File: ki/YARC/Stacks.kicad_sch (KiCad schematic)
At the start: 0 parts

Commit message: Ongoing schematic changes
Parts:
- added U201, U204, U207, U209: 74LS670, symbol 74xx:74LS670
- added U202, U205, U208, U210: 74LS283, symbol 74xx:74LS283
- added U203, U206: 74LS574, symbol 74xx:74LS574
- added U211, U212, U213, U214: 74LS245, symbol 74xx:74LS245
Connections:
- new net: U208.9 (C4), U210.7 (C0)
- new net: U202.9 (C4), U205.7 (C0)
- new net ACN0: U201.14 (Wa), U201.5 (Ra), U204.14 (Wa), U204.5 (Ra), U207.14 (Wa), U207.5 (Ra), U209.14 (Wa), U209.5 (Ra)
- new net ACN1: U201.13 (Wb), U201.4 (Rb), U204.13 (Wb), U204.4 (Rb), U207.13 (Wb), U207.4 (Rb), U209.13 (Wb), U209.4 (Rb)
- new net ALUOUT0: U211.2 (A0)
- new net ALUOUT1: U211.3 (A1)
- new net ALUOUT10: U212.4 (A2)
- new net ALUOUT11: U212.5 (A3)
- new net ALUOUT12: U212.6 (A4)
- new net ALUOUT13: U212.7 (A5)
- new net ALUOUT14: U212.8 (A6)
- new net ALUOUT15: U212.9 (A7)
- new net ALUOUT2: U211.4 (A2)
- new net ALUOUT3: U211.5 (A3)
- new net ALUOUT4: U211.6 (A4)
- new net ALUOUT5: U211.7 (A5)
- new net ALUOUT6: U211.8 (A6)
- new net ALUOUT7: U211.9 (A7)
- new net ALUOUT8: U212.2 (A0)
- new net ALUOUT9: U212.3 (A1)
- new net C8: U205.9 (C4), U208.7 (C0)
- new net GND: U201.8 (GND), U202.7 (C0), U202.8 (GND), U203.1 (OE), U203.10 (GND), U204.8 (GND), U205.8 (GND), U206.1 (OE), U206.10 (GND), U207.8 (GND), U208.8 (GND), U209.8 (GND), U210.8 (GND), U211.10 (GND), U212.10 (GND), U213.10 (GND), U214.10 (GND)
- new net HOLD0: U201.15 (D1), U203.19 (Q0)
- new net HOLD1: U201.1 (D2), U203.18 (Q1)
- new net HOLD10: U206.17 (Q2), U207.2 (D3)
- new net HOLD11: U206.16 (Q3), U207.3 (D4)
- new net HOLD12: U206.15 (Q4), U209.15 (D1)
- new net HOLD13: U206.14 (Q5), U209.1 (D2)
- new net HOLD14: U206.13 (Q6), U209.2 (D3)
- new net HOLD15: U206.12 (Q7), U209.3 (D4)
- new net HOLD2: U201.2 (D3), U203.17 (Q2)
- new net HOLD3: U201.3 (D4), U203.16 (Q3)
- new net HOLD4: U203.15 (Q4), U204.15 (D1)
- new net HOLD5: U203.14 (Q5), U204.1 (D2)
- new net HOLD6: U203.13 (Q6), U204.2 (D3)
- new net HOLD7: U203.12 (Q7), U204.3 (D4)
- new net HOLD8: U206.19 (Q0), U207.15 (D1)
- new net HOLD9: U206.18 (Q1), U207.1 (D2)
- new net SRC2:0: U202.6 (B1)
- new net SRC2:1: U202.2 (B2)
- new net SRC2:2: U202.11 (B4), U202.15 (B3), U205.11 (B4), U205.15 (B3), U205.2 (B2), U205.6 (B1), U208.11 (B4), U208.15 (B3), U208.2 (B2), U208.6 (B1), U210.11 (B4), U210.15 (B3), U210.2 (B2), U210.6 (B1)
- new net SUM0: U202.4 (S1), U203.2 (D0)
- new net SUM1: U202.1 (S2), U203.3 (D1)
- new net SUM10: U206.4 (D2), U208.13 (S3)
- new net SUM11: U206.5 (D3), U208.10 (S4)
- new net SUM12: U206.6 (D4), U210.4 (S1)
- new net SUM13: U206.7 (D5), U210.1 (S2)
- new net SUM14: U206.8 (D6), U210.13 (S3)
- new net SUM15: U206.9 (D7), U210.10 (S4)
- new net SUM2: U202.13 (S3), U203.4 (D2)
- new net SUM3: U202.10 (S4), U203.5 (D3)
- new net SUM4: U203.6 (D4), U205.4 (S1)
- new net SUM5: U203.7 (D5), U205.1 (S2)
- new net SUM6: U203.8 (D6), U205.13 (S3)
- new net SUM7: U203.9 (D7), U205.10 (S4)
- new net SUM8: U206.2 (D0), U208.4 (S1)
- new net SUM9: U206.3 (D1), U208.1 (S2)
- new net SYSADDR0: U201.10 (Q1), U202.5 (A1), U211.18 (B0), U214.11 (B7)
- new net SYSADDR1: U201.9 (Q2), U202.3 (A2), U211.17 (B1), U214.12 (B6)
- new net SYSADDR10: U207.7 (Q3), U208.14 (A3), U212.16 (B2), U213.13 (B5)
- new net SYSADDR11: U207.6 (Q4), U208.12 (A4), U212.15 (B3), U213.14 (B4)
- new net SYSADDR12: U209.10 (Q1), U210.5 (A1), U212.14 (B4), U213.15 (B3)
- new net SYSADDR13: U209.9 (Q2), U210.3 (A2), U212.13 (B5), U213.16 (B2)
- new net SYSADDR14: U209.7 (Q3), U210.14 (A3), U212.12 (B6), U213.17 (B1)
- new net SYSADDR15: U209.6 (Q4), U210.12 (A4), U212.11 (B7), U213.18 (B0)
- new net SYSADDR2: U201.7 (Q3), U202.14 (A3), U211.16 (B2), U214.13 (B5)
- new net SYSADDR3: U201.6 (Q4), U202.12 (A4), U211.15 (B3), U214.14 (B4)
- new net SYSADDR4: U204.10 (Q1), U205.5 (A1), U211.14 (B4), U214.15 (B3)
- new net SYSADDR5: U204.9 (Q2), U205.3 (A2), U211.13 (B5), U214.16 (B2)
- new net SYSADDR6: U204.7 (Q3), U205.14 (A3), U211.12 (B6), U214.17 (B1)
- new net SYSADDR7: U204.6 (Q4), U205.12 (A4), U211.11 (B7), U214.18 (B0)
- new net SYSADDR8: U207.10 (Q1), U208.5 (A1), U212.18 (B0), U213.11 (B7)
- new net SYSADDR9: U207.9 (Q2), U208.3 (A2), U212.17 (B1), U213.12 (B6)
- new net SYSCLK: U203.11 (Cp), U206.11 (Cp)
- new net SYSDATA0: U214.9 (A7)
- new net SYSDATA1: U214.8 (A6)
- new net SYSDATA10: U213.7 (A5)
- new net SYSDATA11: U213.6 (A4)
- new net SYSDATA12: U213.5 (A3)
- new net SYSDATA13: U213.4 (A2)
- new net SYSDATA14: U213.3 (A1)
- new net SYSDATA15: U213.2 (A0)
- new net SYSDATA2: U214.7 (A5)
- new net SYSDATA3: U214.6 (A4)
- new net SYSDATA4: U214.5 (A3)
- new net SYSDATA5: U214.4 (A2)
- new net SYSDATA6: U214.3 (A1)
- new net SYSDATA7: U214.2 (A0)
- new net SYSDATA8: U213.9 (A7)
- new net SYSDATA9: U213.8 (A6)
- new net VCC: U201.16 (VCC), U202.16 (VCC), U203.20 (VCC), U204.16 (VCC), U205.16 (VCC), U206.20 (VCC), U207.16 (VCC), U208.16 (VCC), U209.16 (VCC), U210.16 (VCC), U211.1 (A->B), U211.20 (VCC), U212.1 (A->B), U212.20 (VCC), U213.1 (A->B), U213.20 (VCC), U214.1 (A->B), U214.20 (VCC)
- new net ~{ALUtoA}: U211.19 (CE), U212.19 (CE)
- new net ~{DtoA}: U213.19 (CE), U214.19 (CE)
- new net ~{IXRD}: U201.11 (~{Er}), U204.11 (~{Er}), U207.11 (~{Er}), U209.11 (~{Er})
- new net ~{IXWR}: U201.12 (~{Ew}), U204.12 (~{Ew}), U207.12 (~{Ew}), U209.12 (~{Ew})
- no-connect marks 0 -> 1
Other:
- note added: "The U200-numbered ICs on this page match the low digits of the U numbers on the V503 Addressing Unit circuit board. U207 on this page is U7 on the circuit board, etc. Other names match the V503 schematic where possible but all match the naming here in the YARC schematic."
- title: YARC Stacks -> YARC Addressing Unit (AU)

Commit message: Schematic for addressing unit is complete and all ERC violations addressed
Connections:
- net ~{ALUtoA} renamed ~{ADDR_ALU}
- net ~{DtoA} renamed ~{SYSDATA_SRC_IS_A}

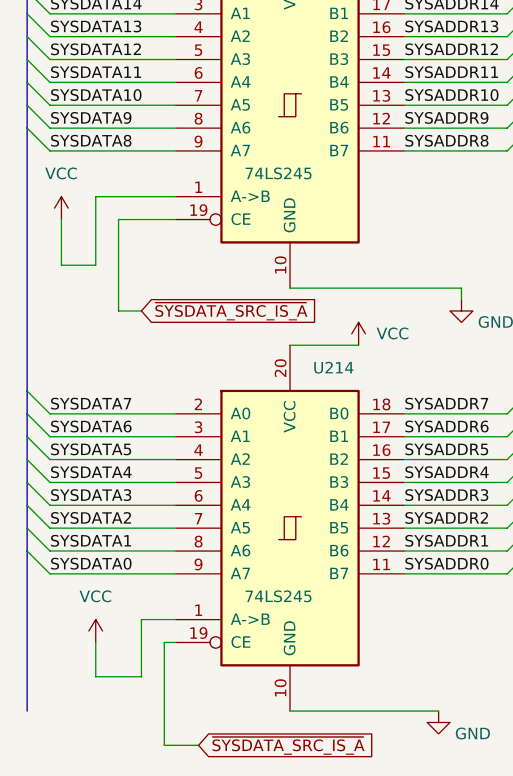
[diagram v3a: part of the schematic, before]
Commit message: Revise SET# logic for LD_UCODE_CTR#. Fix minor errors with no functional consequences (schematic didn't match reality)
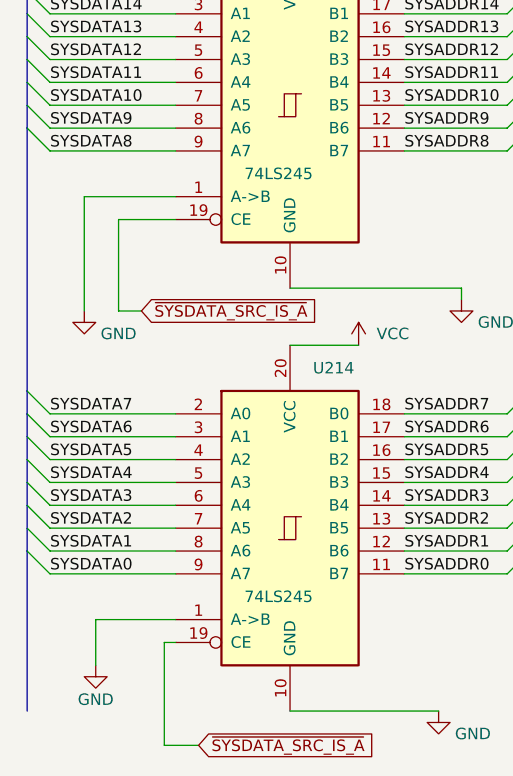
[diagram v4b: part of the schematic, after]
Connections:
- net GND: now also U213.1 (A->B), U214.1 (A->B)
- net VCC: no longer U213.1 (A->B), U214.1 (A->B)
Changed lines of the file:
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@@
     (stroke (width 0) (type default))
   )
-  (wire (pts (xy 29.21 187.96) (xy 25.4 187.96))
+  (wire (pts (xy 29.21 187.96) (xy 20.32 187.96))
     (stroke (width 0) (type default))
   )
@@
     (stroke (width 0) (type default))
   )
-  (wire (pts (xy 20.32 140.97) (xy 20.32 148.59))
-    (stroke (width 0) (type default))
-  )
   (bus (pts (xy 207.01 72.39) (xy 207.01 74.93))
     (stroke (width 0) (type default))
@@
     (stroke (width 0) (type default))
   )
-  (wire (pts (xy 20.32 148.59) (xy 16.51 148.59))
-    (stroke (width 0) (type default))
-  )
   (bus (pts (xy 12.7 172.72) (xy 12.7 175.26))
     (stroke (width 0) (type default))
@@
     (stroke (width 0) (type default))
   )
+  (wire (pts (xy 19.05 140.97) (xy 19.05 153.67))
+    (stroke (width 0) (type default))
+  )
   (wire (pts (xy 173.99 116.84) (xy 173.99 129.54))
     (stroke (width 0) (type default))
@@
     (stroke (width 0) (type default))
   )
-  (wire (pts (xy 16.51 143.51) (xy 16.51 148.59))
-    (stroke (width 0) (type default))
-  )
   (bus (pts (xy 147.32 25.4) (xy 147.32 27.94))
     (stroke (width 0) (type default))
@@
     (stroke (width 0) (type default))
   )
-  (wire (pts (xy 20.32 190.5) (xy 20.32 194.31))
-    (stroke (width 0) (type default))
-  )
   (wire (pts (xy 15.24 133.35) (xy 29.21 133.35))
     (stroke (width 0) (type default))
@@
     (stroke (width 0) (type default))
   )
-  (wire (pts (xy 25.4 187.96) (xy 25.4 194.31))
+  (wire (pts (xy 20.32 187.96) (xy 20.32 193.04))
     (stroke (width 0) (type default))
   )
@@
     (stroke (width 0) (type default))
   )
-  (wire (pts (xy 20.32 140.97) (xy 29.21 140.97))
+  (wire (pts (xy 19.05 140.97) (xy 29.21 140.97))
     (stroke (width 0) (type default))
   )
@@
   )
   (bus (pts (xy 266.7 25.4) (xy 266.7 27.94))
-    (stroke (width 0) (type default))
-  )
-  (wire (pts (xy 25.4 194.31) (xy 20.32 194.31))
     (stroke (width 0) (type default))
   )
@@
     )
   )
+  (symbol (lib_id "power:GND") (at 19.05 153.67 0) (unit 1)
+    (in_bom yes) (on_board yes) (dnp no)
+    (property "Reference" "#PWR0249" (at 19.05 160.02 0)
+      (effects (font (size 1.27 1.27)) hide)
+    )
+    (property "Value" "GND" (at 22.86 156.21 0)
+      (effects (font (size 1.27 1.27)))
+    )
+    (property "Footprint" "" (at 19.05 153.67 0)
+      (effects (font (size 1.27 1.27)) hide)
+    )
+    (property "Datasheet" "" (at 19.05 153.67 0)
+      (effects (font (size 1.27 1.27)) hide)
+    )
+    (pin "1")
+    (instances
+      (project "YARC"
+        (path "/22e0f8e1-b0d7-4d47-bb7c-8ef04cd95fca/ab31a2b6-5416-47ce-a658-779ff6faeebe"
+          (reference "#PWR0249") (unit 1)
+        )
+      )
+    )
+  )
   (symbol (lib_id "power:GND") (at 232.41 63.5 0) (unit 1)
     (in_bom yes) (on_board yes) (dnp no) (fields_autoplaced)
@@
     )
   )
+  (symbol (lib_id "power:GND") (at 20.32 193.04 0) (unit 1)
+    (in_bom yes) (on_board yes) (dnp no)
+    (property "Reference" "#PWR0160" (at 20.32 199.39 0)
+      (effects (font (size 1.27 1.27)) hide)
+    )
+    (property "Value" "GND" (at 20.32 196.85 0)
+      (effects (font (size 1.27 1.27)))
+    )
+    (property "Footprint" "" (at 20.32 193.04 0)
+      (effects (font (size 1.27 1.27)) hide)
+    )
+    (property "Datasheet" "" (at 20.32 193.04 0)
+      (effects (font (size 1.27 1.27)) hide)
+    )
+    (pin "1")
+    (instances
+      (project "YARC"
+        (path "/22e0f8e1-b0d7-4d47-bb7c-8ef04cd95fca/ab31a2b6-5416-47ce-a658-779ff6faeebe"
+          (reference "#PWR0160") (unit 1)
+        )
+      )
+    )
+  )
   (symbol (lib_id "power:GND") (at 153.67 143.51 0) (unit 1)
     (in_bom yes) (on_board yes) (dnp no) (fields_autoplaced)
@@
         (path "/22e0f8e1-b0d7-4d47-bb7c-8ef04cd95fca/ab31a2b6-5416-47ce-a658-779ff6faeebe"
           (reference "U210") (unit 1)
-        )
-      )
-    )
-  )
-  (symbol (lib_id "power:VCC") (at 20.32 190.5 0) (unit 1)
-    (in_bom yes) (on_board yes) (dnp no) (fields_autoplaced)
-    (property "Reference" "#PWR0249" (at 20.32 194.31 0)
-      (effects (font (size 1.27 1.27)) hide)
-    )
-    (property "Value" "VCC" (at 20.32 185.42 0)
-      (effects (font (size 1.27 1.27)))
-    )
-    (property "Footprint" "" (at 20.32 190.5 0)
-      (effects (font (size 1.27 1.27)) hide)
-    )
-    (property "Datasheet" "" (at 20.32 190.5 0)
-      (effects (font (size 1.27 1.27)) hide)
-    )
-    (pin "1")
-    (instances
-      (project "YARC"
-        (path "/22e0f8e1-b0d7-4d47-bb7c-8ef04cd95fca/ab31a2b6-5416-47ce-a658-779ff6faeebe"
-          (reference "#PWR0249") (unit 1)
         )
       )
@@
         )
       )
-    )
-  )
-  (symbol (lib_id "power:VCC") (at 16.51 143.51 0) (unit 1)
-    (in_bom yes) (on_board yes) (dnp no) (fields_autoplaced)
-    (property "Reference" "#PWR0250" (at 16.51 147.32 0)
-      (effects (font (size 1.27 1.27)) hide)
-    )
-    (property "Value" "VCC" (at 16.51 138.43 0)
-      (effects (font (size 1.27 1.27)))
-    )
-    (property "Footprint" "" (at 16.51 143.51 0)
-      (effects (font (size 1.27 1.27)) hide)
-    )
-    (property "Datasheet" "" (at 16.51 143.51 0)
-      (effects (font (size 1.27 1.27)) hide)
-    )
-    (pin "1")
-    (instances
-      (project "YARC"
-        (path "/22e0f8e1-b0d7-4d47-bb7c-8ef04cd95fca/ab31a2b6-5416-47ce-a658-779ff6faeebe"
-          (reference "#PWR0250") (unit 1)
-        )
-      )

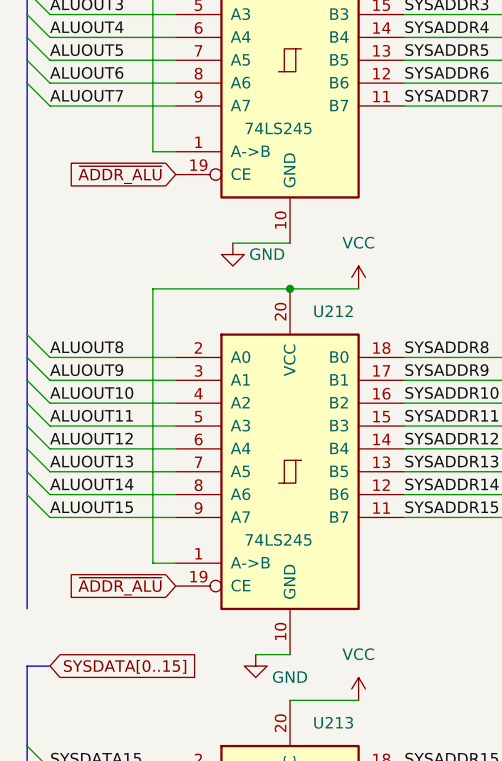
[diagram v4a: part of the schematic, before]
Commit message: Make main schematic match V503 schematic control signal naming and minor layout cleanup
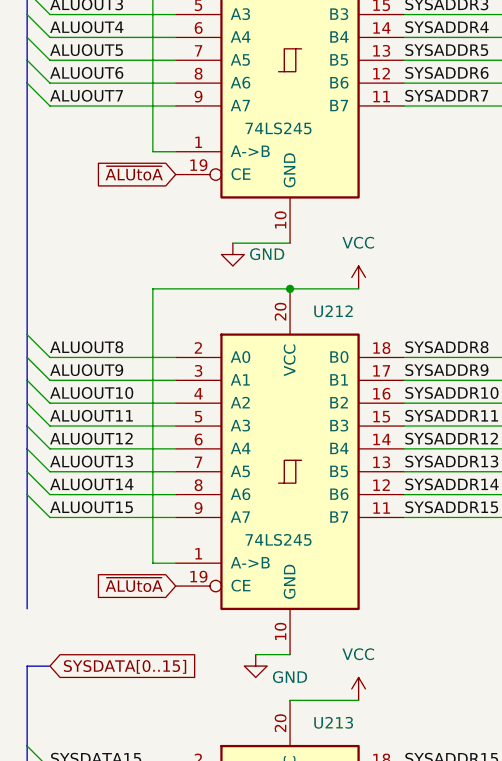
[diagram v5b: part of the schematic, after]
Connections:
- net ~{ADDR_ALU} renamed ~{ALUtoA}
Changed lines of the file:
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@@
     )
   )
-  (global_label "~{ADDR_ALU}" (shape input) (at 29.21 52.07 180) (fields_autoplaced)
+  (global_label "~{ALUtoA}" (shape input) (at 29.21 52.07 180) (fields_autoplaced)
     (effects (font (size 1.27 1.27)) (justify right))
-    (property "Intersheetrefs" "${INTERSHEET_REFS}" (at 16.9114 52.07 0)
+    (property "Intersheetrefs" "${INTERSHEET_REFS}" (at 19.8143 52.07 0)
       (effects (font (size 1.27 1.27)) (justify right) hide)
     )
@@
     )
   )
-  (global_label "~{ADDR_ALU}" (shape input) (at 29.21 97.79 180) (fields_autoplaced)
+  (global_label "~{ALUtoA}" (shape input) (at 29.21 97.79 180) (fields_autoplaced)
     (effects (font (size 1.27 1.27)) (justify right))
-    (property "Intersheetrefs" "${INTERSHEET_REFS}" (at 16.9114 97.79 0)
+    (property "Intersheetrefs" "${INTERSHEET_REFS}" (at 19.8143 97.79 0)
       (effects (font (size 1.27 1.27)) (justify right) hide)
     )
